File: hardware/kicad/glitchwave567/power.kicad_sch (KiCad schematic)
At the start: 39 parts, among them J5 DC_2.1mm, Q10 AO3401A, Q11 BCP56, U11 L78L09, U12 MP1584EN, U6 TL074

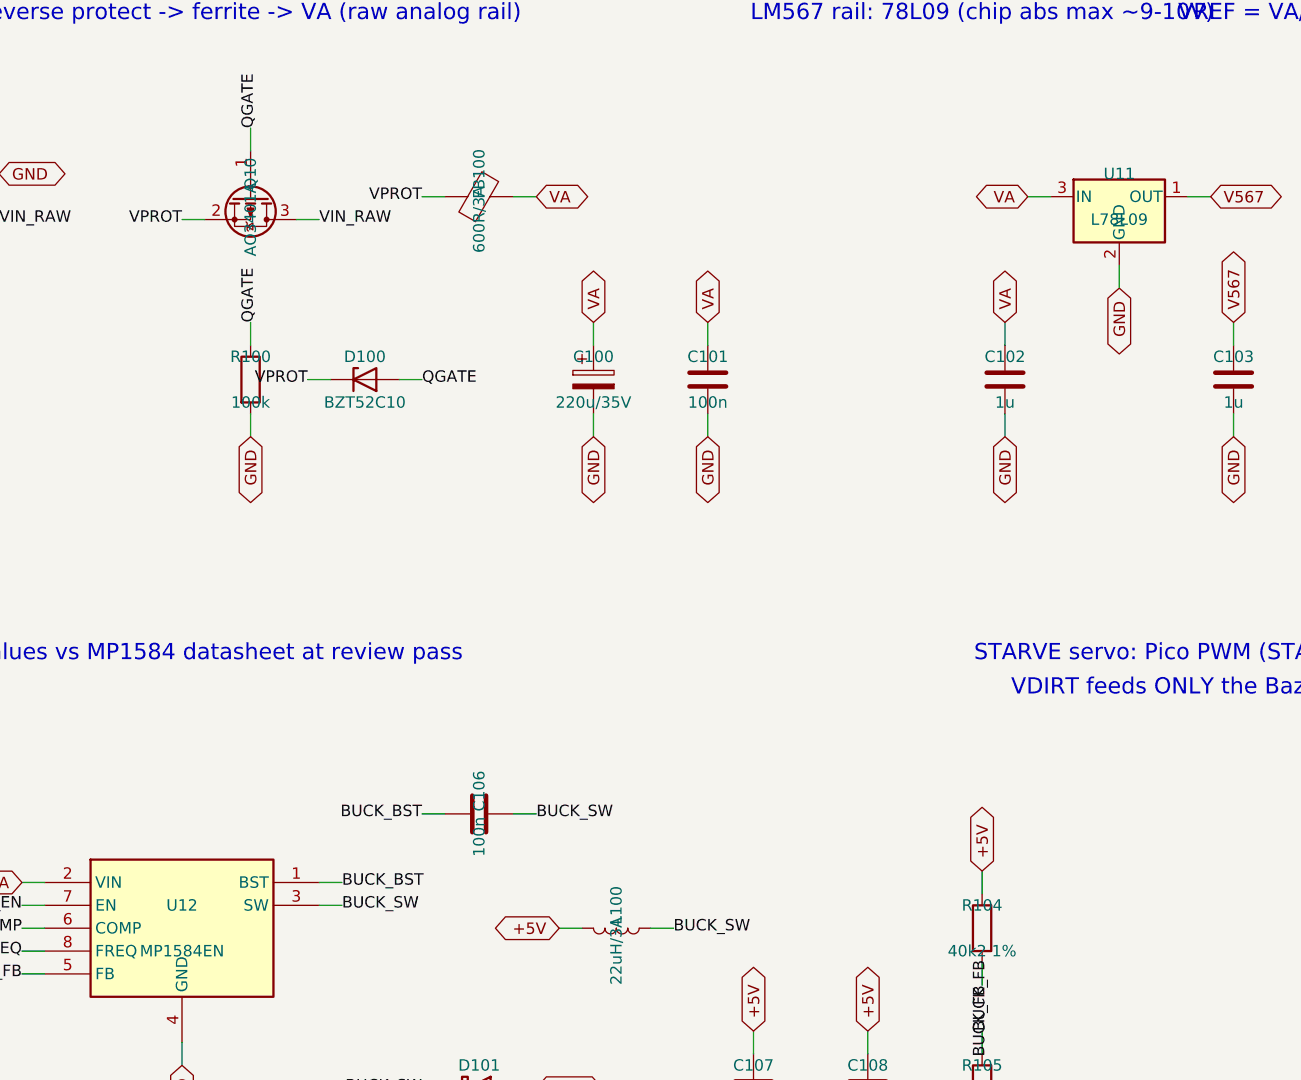
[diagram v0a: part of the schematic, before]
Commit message: hardware: root hierarchy + ERC pass on KiCad 10 (down to lib-mismatch/footprint noise + 2 intentional OTA current-sum waivers)
- root sheet ties all 8 sheets into one project (global-label connectivity, 288 comps / 259 nets stitch verified)
- fixed: U11/U12->U18/U19 ref clash, MCU cap ref clashes, env rectifier D81 feedback returned to virtual ground (was floating FW_IN2), PWR_FLAGs on PICO_VSYS + ctrl rails, off-grid buffer pin
- remaining ERC: footprint_link (assignment pending), lib_symbol_mismatch (v6 embedded vs v10 libs, cosmetic), 2x pin_to_pin Output-Output = LM13700 current summing (by design, noted on sheets)

Co-Authored-By: Claude Fable 5 <noreply@anthropic.com>
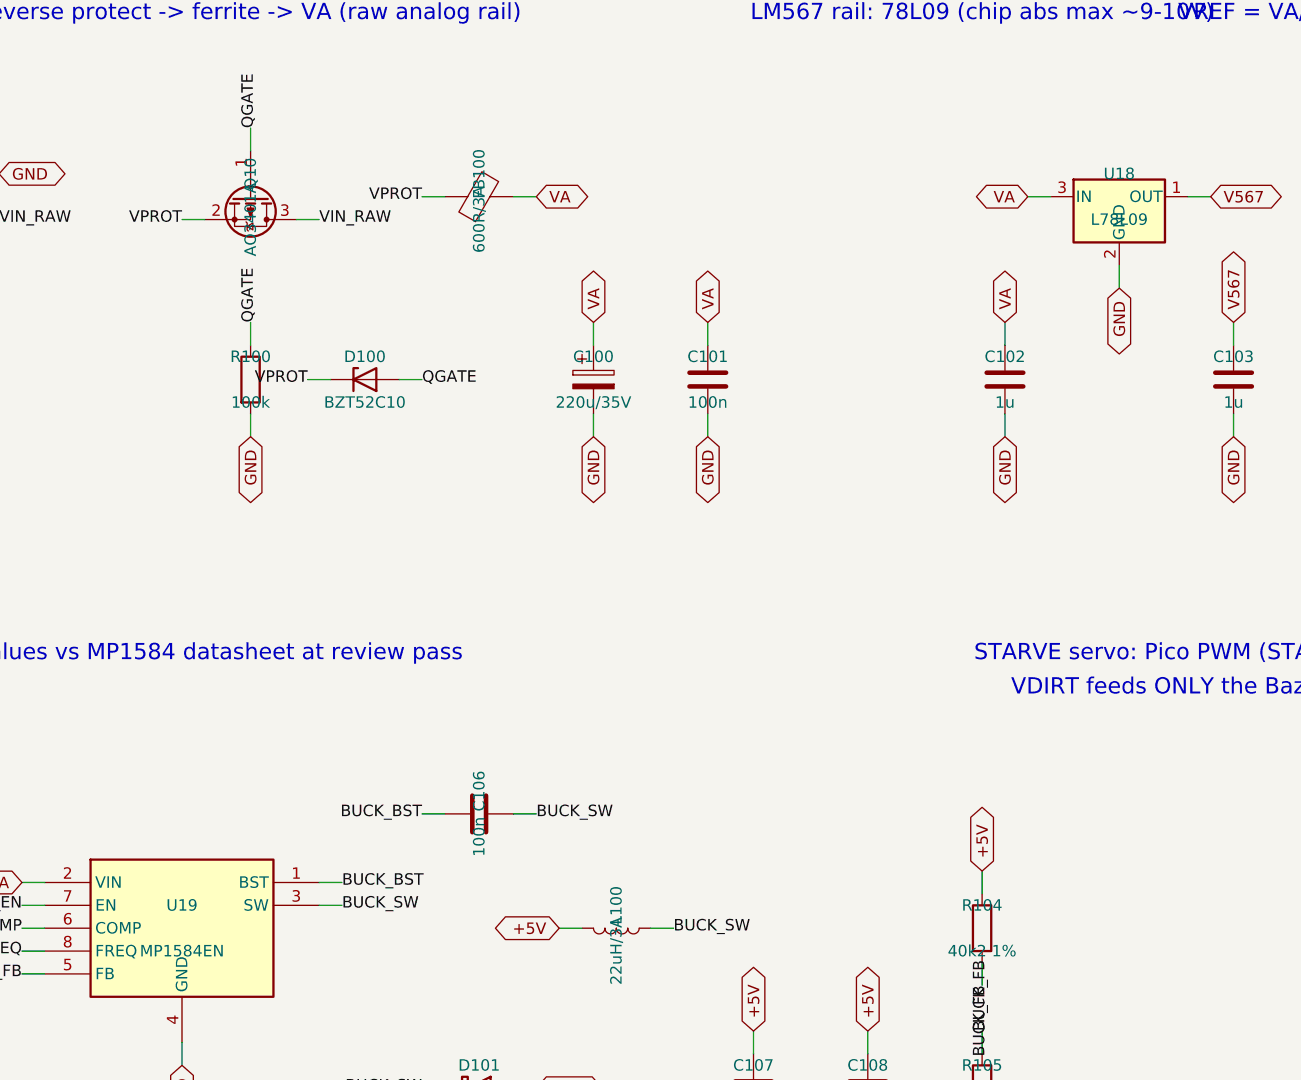
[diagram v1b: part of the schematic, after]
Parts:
- removed U11: L78L09, symbol Regulator_Linear:L78L09_SOT89
- removed U12: MP1584EN, symbol Glitchwave:MP1584EN
- added U18: L78L09, symbol Regulator_Linear:L78L09_SOT89
- added U19: MP1584EN, symbol Glitchwave:MP1584EN
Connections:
- net BUCK_BST: now also U19.1 (BST)
- net BUCK_COMP: now also U19.6 (COMP)
- net BUCK_EN: now also U19.7 (EN)
- net BUCK_FB: now also U19.5 (FB)
- net BUCK_FREQ: now also U19.8 (FREQ)
- net BUCK_SW: now also U19.3 (SW)
- net GND: now also U18.2 (GND), U19.4 (GND)
- net V567: now also U18.1 (OUT)
- net VA: now also U18.3 (IN), U19.2 (VIN)
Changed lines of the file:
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@@
   (symbol (lib_id "Regulator_Linear:L78L09_SOT89") (at 167.64 45.72 0) (unit 1)
     (in_bom yes) (on_board yes) (dnp no)
-    (property "Reference" "U11" (id 0) (at 167.64 43.18 0)
+    (property "Reference" "U18" (id 0) (at 167.64 43.18 0)
       (effects (font (size 1.27 1.27)))
     )
@@
       (project "glitchwave567"
         (path "/"
-          (reference "U11") (unit 1)
+          (reference "U18") (unit 1)
         )
       )
@@
   (symbol (lib_id "Glitchwave:MP1584EN") (at 63.5 127.0 0) (unit 1)
     (in_bom yes) (on_board yes) (dnp no)
-    (property "Reference" "U12" (id 0) (at 63.5 124.46 0)
+    (property "Reference" "U19" (id 0) (at 63.5 124.46 0)
       (effects (font (size 1.27 1.27)))
     )
@@
       (project "glitchwave567"
         (path "/"
-          (reference "U12") (unit 1)
+          (reference "U19") (unit 1)
         )
       )

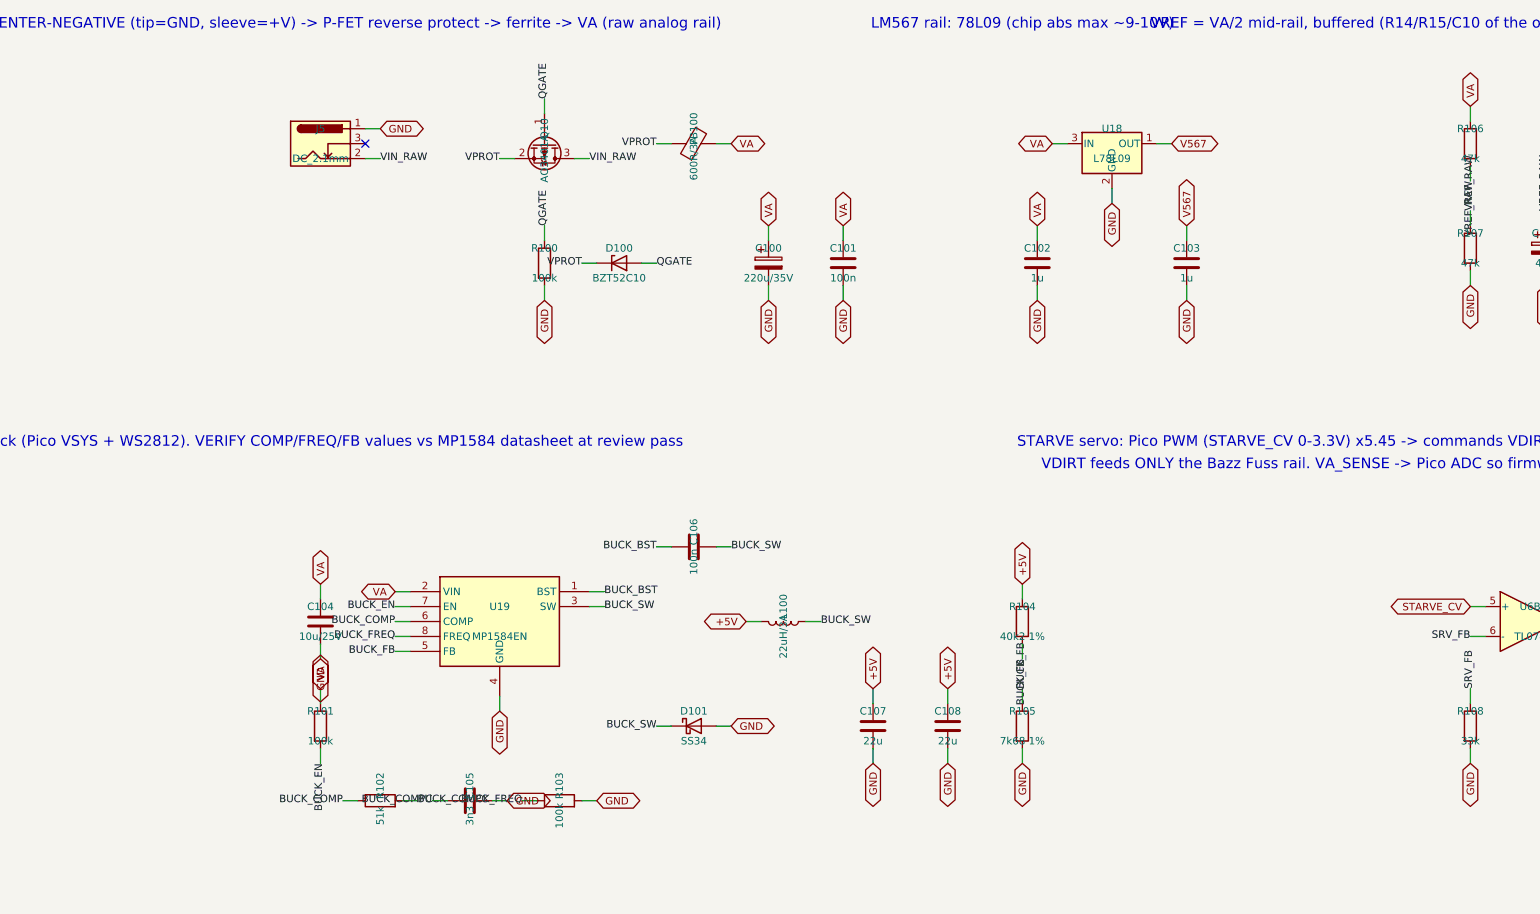
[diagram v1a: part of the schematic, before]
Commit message: hardware: datasheet review pass - 13 fixes incl. 2 fatal (MP1584 pin scramble, SVF feedback dividers)
HIGH: MP1584 symbol pins remapped to real SOIC-8; EN divider 24k9 added (18V
on a 6V-max pin); SVF integrator 220k/680 feedback dividers + 220p caps
(was tuning to 611kHz); LM13700 buffer 10k DC loads; 78L09->1N4148W drop
(LM567C 9V abs max); bell EQ redesigned (was electrically inert - now exact
+3.04dB@790Hz Q=0.500); Pico ADC_VREF external feed removed (onboard ref).
MED: FREQ_CV 2nd PWM pole (-112dB, pitch FM), env attack 3.9k (exact 4ms),
567 pin3 1k clamp limit, SMAJ18A on VA, 50V input cap, buffer parking.
Full report: hardware/SCHEMATIC_REVIEW.md. All sheets re-verified.

Co-Authored-By: Claude Fable 5 <noreply@anthropic.com>
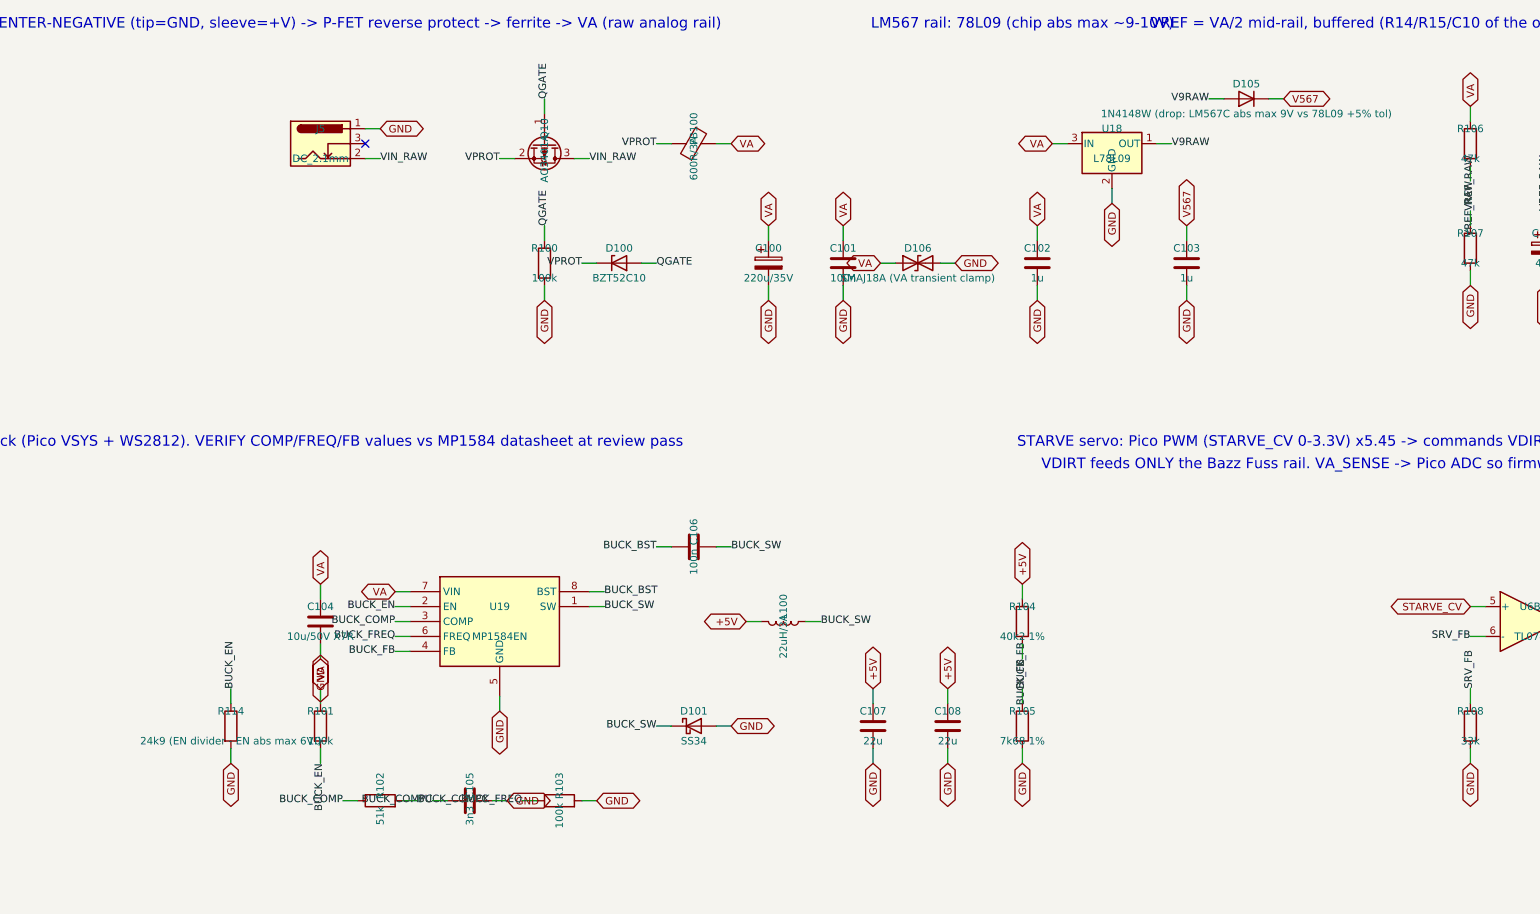
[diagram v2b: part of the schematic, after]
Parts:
- added D105: 1N4148W (drop: LM567C abs max 9V vs 78L09 +5% tol), symbol Device:D
- added D106: SMAJ18A (VA transient clamp), symbol Device:D_TVS
- added R114: 24k9 (EN divider - EN abs max 6V!), symbol Device:R
- C104: value 10u/25V -> 10u/50V X7R
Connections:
- net BUCK_BST: now also U19.8 (BST); no longer U19.1 (BST)
- net BUCK_COMP: now also U19.3 (COMP); no longer U19.6 (COMP)
- net BUCK_EN: now also U19.2 (EN), R114.1; no longer U19.7 (EN)
- net BUCK_FB: now also U19.4 (FB); no longer U19.5 (FB)
- net BUCK_FREQ: now also U19.6 (FREQ); no longer U19.8 (FREQ)
- net BUCK_SW: now also U19.1 (SW); no longer U19.3 (SW)
- net GND: now also U19.5 (GND), D106.2 (A2), R114.2; no longer U19.4 (GND)
- net V567: now also D105.1 (K); no longer U18.1 (OUT)
- net VA: now also U19.7 (VIN), D106.1 (A1); no longer U19.2 (VIN)
- new net V9RAW: D105.2 (A), U18.1 (OUT)
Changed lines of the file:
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@@
+    (stroke (width 0.0))
+  )
+  (wire (pts (xy 130.81 66.04) (xy 128.27 66.04))
+    (stroke (width 0.0))
+  )
+  (wire (pts (xy 138.43 66.04) (xy 140.97 66.04))
     (stroke (width 0.0))
   )
@@
     (stroke (width 0.0))
   )
+  (wire (pts (xy 186.69 38.1) (xy 184.15 38.1))
+    (stroke (width 0.0))
+  )
+  (wire (pts (xy 194.31 38.1) (xy 196.85 38.1))
+    (stroke (width 0.0))
+  )
   (wire (pts (xy 154.94 62.23) (xy 154.94 59.69))
     (stroke (width 0.0))
@@
   )
   (wire (pts (xy 33.02 148.59) (xy 33.02 151.13))
+    (stroke (width 0.0))
+  )
+  (wire (pts (xy 17.78 140.97) (xy 17.78 138.43))
+    (stroke (width 0.0))
+  )
+  (wire (pts (xy 17.78 148.59) (xy 17.78 151.13))
     (stroke (width 0.0))
   )
@@
     (effects (font (size 1.27 1.27)))
   )
+  (label "V9RAW" (at 177.8 45.72 0)
+    (effects (font (size 1.27 1.27)))
+  )
+  (label "V9RAW" (at 184.15 38.1 180)
+    (effects (font (size 1.27 1.27)))
+  )
   (label "BUCK_EN" (at 45.72 124.46 180)
     (effects (font (size 1.27 1.27)))
@@
     (effects (font (size 1.27 1.27)))
   )
+  (label "BUCK_EN" (at 17.78 138.43 90)
+    (effects (font (size 1.27 1.27)))
+  )
   (label "BUCK_COMP" (at 36.83 157.48 180)
     (effects (font (size 1.27 1.27)))
@@
     (effects (font (size 1.27 1.27)))
   )
+  (global_label "VA" (shape bidirectional) (at 128.27 66.04 180)
+    (effects (font (size 1.27 1.27)))
+  )
+  (global_label "GND" (shape bidirectional) (at 140.97 66.04 0)
+    (effects (font (size 1.27 1.27)))
+  )
   (global_label "VA" (shape bidirectional) (at 157.48 45.72 180)
     (effects (font (size 1.27 1.27)))
   )
-  (global_label "V567" (shape bidirectional) (at 177.8 45.72 0)
-    (effects (font (size 1.27 1.27)))
-  )
   (global_label "GND" (shape bidirectional) (at 167.64 55.88 270)
     (effects (font (size 1.27 1.27)))
   )
+  (global_label "V567" (shape bidirectional) (at 196.85 38.1 0)
+    (effects (font (size 1.27 1.27)))
+  )
   (global_label "VA" (shape bidirectional) (at 154.94 59.69 90)
     (effects (font (size 1.27 1.27)))
@@
     (effects (font (size 1.27 1.27)))
   )
+  (global_label "GND" (shape bidirectional) (at 17.78 151.13 270)
+    (effects (font (size 1.27 1.27)))
+  )
   (global_label "GND" (shape bidirectional) (at 64.77 157.48 0)
     (effects (font (size 1.27 1.27)))
@@
     )
   )
+  (symbol (lib_id "Device:D_TVS") (at 134.62 66.04 0) (unit 1)
+    (in_bom yes) (on_board yes) (dnp no)
+    (property "Reference" "D106" (id 0) (at 134.62 63.50000000000001 0)
+      (effects (font (size 1.27 1.27)))
+    )
+    (property "Value" "SMAJ18A (VA transient clamp)" (id 1) (at 134.62 68.58000000000001 0)
+      (effects (font (size 1.27 1.27)))
+    )
+    (property "Footprint" "" (id 2) (at 134.62 66.04 0)
+      (effects (font (size 1.27 1.27)) hide)
+    )
+    (property "Datasheet" "" (id 3) (at 134.62 66.04 0)
+      (effects (font (size 1.27 1.27)) hide)
+    )
+    (instances
+      (project "glitchwave567"
+        (path "/"
+          (reference "D106") (unit 1)
+        )
+      )
+    )
+  )
   (symbol (lib_id "Regulator_Linear:L78L09_SOT89") (at 167.64 45.72 0) (unit 1)
     (in_bom yes) (on_board yes) (dnp no)
@@
     )
   )
+  (symbol (lib_id "Device:D") (at 190.5 38.1 180) (unit 1)
+    (in_bom yes) (on_board yes) (dnp no)
+    (property "Reference" "D105" (id 0) (at 190.5 35.56 0)
+      (effects (font (size 1.27 1.27)))
+    )
+    (property "Value" "1N4148W (drop: LM567C abs max 9V vs 78L09 +5% tol)" (id 1) (at 190.5 40.64 0)
+      (effects (font (size 1.27 1.27)))
+    )
+    (property "Footprint" "" (id 2) (at 190.5 38.1 0)
+      (effects (font (size 1.27 1.27)) hide)
+    )
+    (property "Datasheet" "" (id 3) (at 190.5 38.1 0)
+      (effects (font (size 1.27 1.27)) hide)
+    )
+    (instances
+      (project "glitchwave567"
+        (path "/"
+          (reference "D105") (unit 1)
+        )
+      )
+    )
+  )
   (symbol (lib_id "Device:C") (at 154.94 66.04 0) (unit 1)
     (in_bom yes) (on_board yes) (dnp no)
@@
       (effects (font (size 1.27 1.27)))
     )
-    (property "Value" "10u/25V" (id 1) (at 33.02 129.54 0)
+    (property "Value" "10u/50V X7R" (id 1) (at 33.02 129.54 0)
       (effects (font (size 1.27 1.27)))
     )
@@
         )
       )
+    )
+  )
+  (symbol (lib_id "Device:R") (at 17.78 144.78 0) (unit 1)
+    (in_bom yes) (on_board yes) (dnp no)
+    (property "Reference" "R114" (id 0) (at 17.78 142.24 0)
+      (effects (font (size 1.27 1.27)))
+    )
+    (property "Value" "24k9 (EN divider - EN abs max 6V!)" (id 1) (at 17.78 147.32 0)
+      (effects (font (size 1.27 1.27)))
+    )
+    (property "Footprint" "" (id 2) (at 17.78 144.78 0)
+      (effects (font (size 1.27 1.27)) hide)
+    )
+    (property "Datasheet" "" (id 3) (at 17.78 144.78 0)
+      (effects (font (size 1.27 1.27)) hide)
+    )
+    (instances
+      (project "glitchwave567"
+        (path "/"
+          (reference "R114") (unit 1)
+        )
+      )

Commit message: hardware: footprint phase complete - 297/297 parts footprinted, custom Glitchwave.pretty authored from factory drawings
- Glitchwave.pretty: PJ-603A (pads 7.6/15.1/22.5, slots per HY-WI-32), PJ-3410,
  DC-044A (polarity DMM-verify flagged), ALPS_RK09K1130 (2.5 pitch + 8.8 snap
  legs from ALPS drawing), SSWFS-S01 (slot pads absorb 5.5-6.5 pin-spacing
  ambiguity; NOTE: PC-pin variant thread is 15/32-32 - panel hole D12.2+keyway,
  not M12), RPi_Pico_SMD (official Fig.5 land pattern, row c-c 19.38)
- schgen auto-footprint map wired into add(); all sheets regenerated
- fp-lib-tables for both projects; trims -> Bourns 3224W; clamps -> 1N5819W

Co-Authored-By: Claude Fable 5 <noreply@anthropic.com>
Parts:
- C100: footprint (none) -> Capacitor_SMD:CP_Elec_8x10.2
- C101, C102, C103, C105, C106, C111: footprint (none) -> Capacitor_SMD:C_0603_1608Metric
- C104: footprint (none) -> Capacitor_SMD:C_1206_3216Metric
- C107, C108: footprint (none) -> Capacitor_SMD:C_0805_2012Metric
- C109, C110: footprint (none) -> Capacitor_SMD:CP_Elec_6.3x5.4
- D100, D102, D103, D104, D105: footprint (none) -> Diode_SMD:D_SOD-123
- D101, D106: footprint (none) -> Diode_SMD:D_SMA
- FB100: footprint (none) -> Inductor_SMD:L_1206_3216Metric
- J5: footprint (none) -> Glitchwave:DC-044A
- L100: footprint (none) -> Inductor_SMD:L_Bourns-SRN8040_8x8.15mm
- Q10: footprint (none) -> Package_TO_SOT_SMD:SOT-23
- Q11: footprint (none) -> Package_TO_SOT_SMD:SOT-223-3_TabPin2
- R100, R101, R102, R103, R104, R105, R106, R107, R108, R109, R110, R111, R112, R113, R114: footprint (none) -> Resistor_SMD:R_0603_1608Metric
- U18: footprint (none) -> Package_TO_SOT_SMD:SOT-89-3
- U19: footprint (none) -> Package_SO:SOIC-8-1EP_3.9x4.9mm_P1.27mm_EP2.29x3mm
- U6: footprint (none) -> Package_SO:SOIC-14_3.9x8.7mm_P1.27mm
